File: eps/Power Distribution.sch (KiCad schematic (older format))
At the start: 87 parts, among them Q1 2N7002, Q11 IRF7425, Q12 2N7002, Q13 IRF7425, Q14 IRF7425, Q15 2N7002, Q16 IRF7425, Q17 IRF7425, Q19 IRF7425, Q2 2N7002, Q20 IRF7425, Q21 IRF7425, Q3 IRF7425, Q4 IRF7425, Q5 2N7002, Q6 2N7002, Q9 2N7002, U13 LT6106, U14 LT6106, U15 LT6106, U16 LT6106, U17 LT6106, U18 LT6106, U19 LT6106, U20 LT6106, U21 LT6106

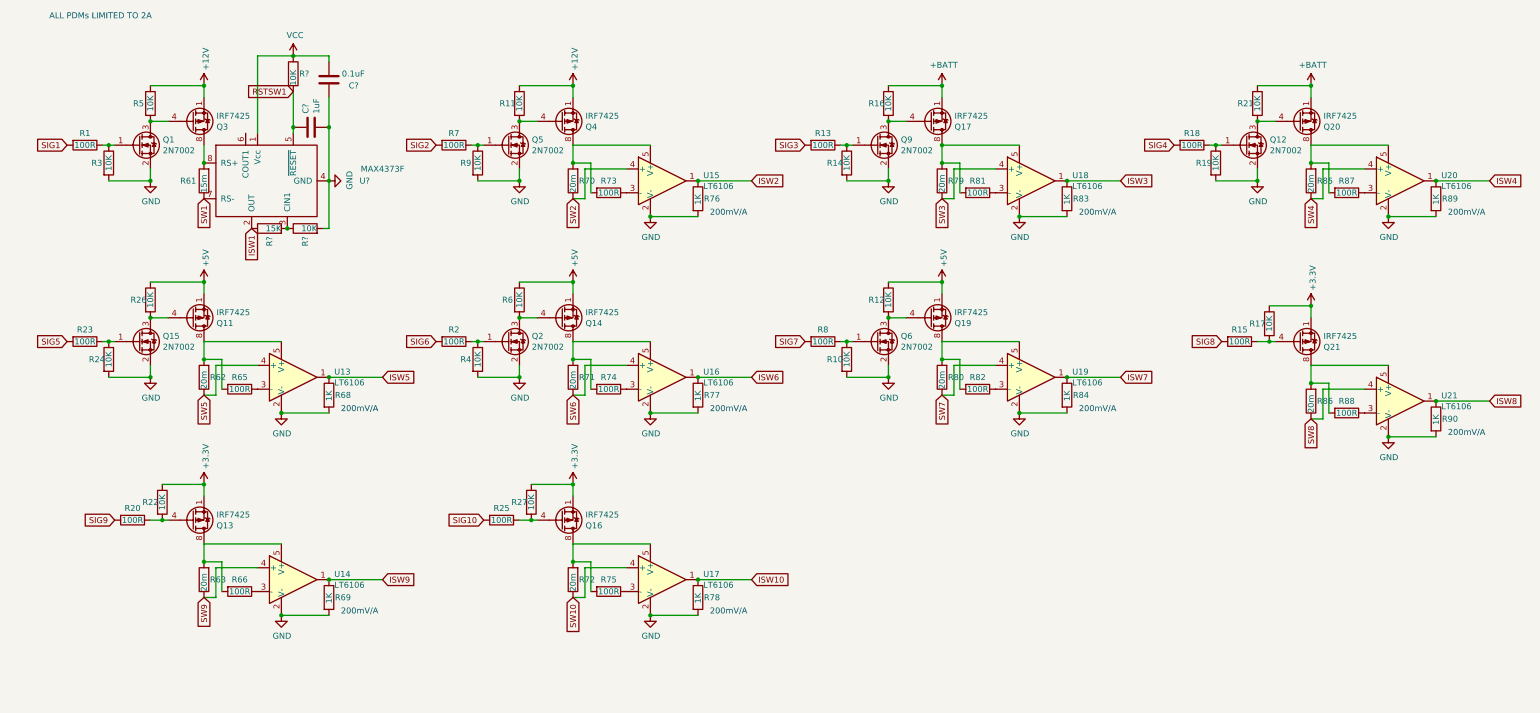
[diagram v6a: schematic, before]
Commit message: implement PDM LCLs
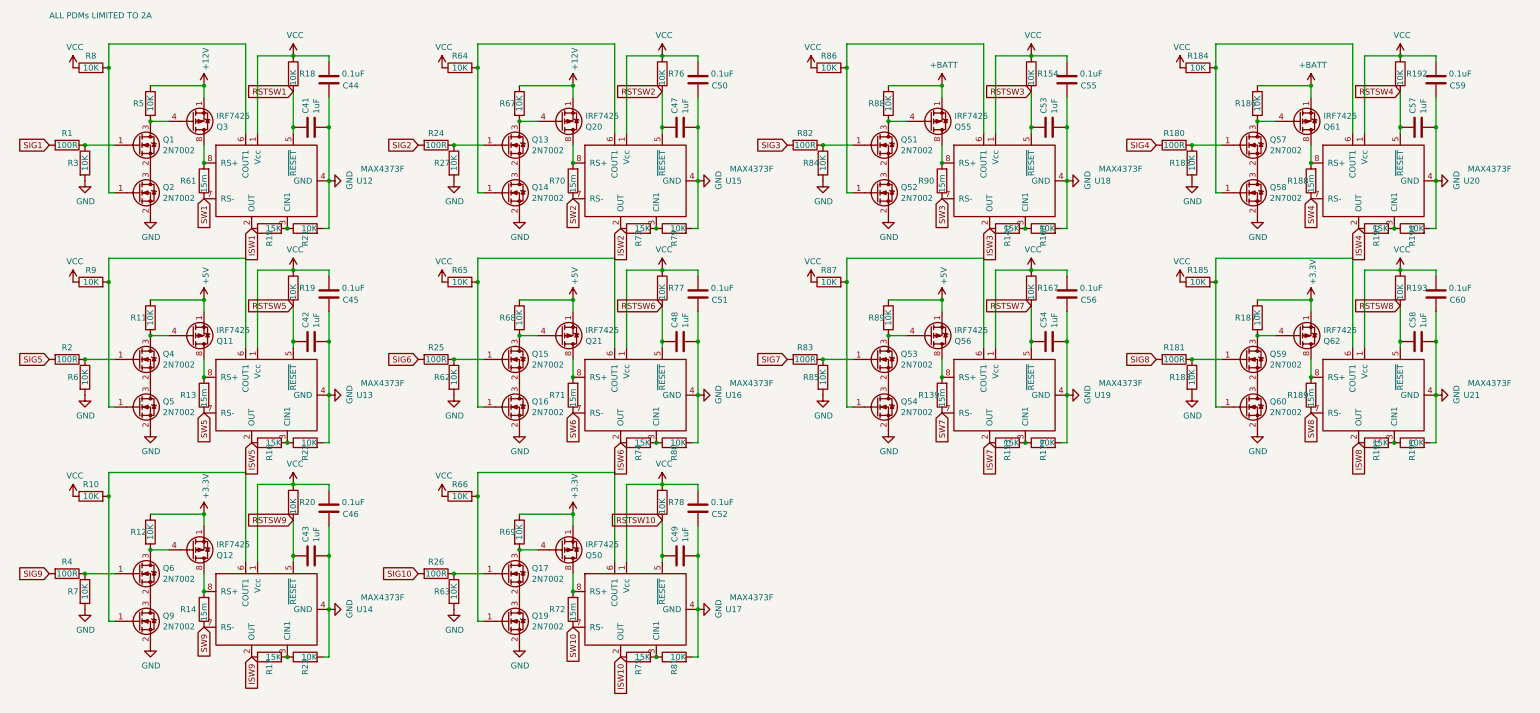
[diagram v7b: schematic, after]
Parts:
- removed Q12: 2N7002, Package_TO_SOT_SMD:SOT-23, symbol Transistor_FET:2N7002
- removed Q13, Q14, Q16, Q17, Q19, Q4: IRF7425, Package_SO:SOIC-8_3.9x4.9mm_P1.27mm, symbol Transistor_FET:IRF7404
- removed R15, R18: 100R, symbol Device:R
- removed R21: 10K, symbol Device:R
- removed U13, U14, U15, U16, U17, U18, U19, U20, U21: LT6106, Package_TO_SOT_SMD:SOT-23-5, symbol Amplifier_Current:LT6106
- added C42, C43, C47, C48, C49, C53, C54, C57, C58: 1uF, symbol Device:C
- added C45, C46, C50, C51, C52, C55, C56, C59, C60: 0.1uF, symbol Device:C
- added Q12, Q50, Q55, Q56, Q61, Q62: IRF7425, Package_SO:SOIC-8_3.9x4.9mm_P1.27mm, symbol Transistor_FET:IRF7404
- added Q13, Q14, Q16, Q17, Q19, Q4, Q51, Q52, Q53, Q54, Q57, Q58, Q59, Q60: 2N7002, Package_TO_SOT_SMD:SOT-23, symbol Transistor_FET:2N7002
- added R139, R188, R189: 15m, symbol Device:R
- added R140, R153, R190, R191: 15K, symbol Device:R
- added R154, R167, R168, R179, R182, R183, R184, R185, R186, R187, R192, R193, R194, R195, R64, R67: 10K, symbol Device:R
- added R180, R181: 100R, symbol Device:R
- added U13, U14, U15, U16, U17, U18, U19, U20, U21: MAX4373F, symbol epslib:MAX4373
- R13: value 100R -> 15m
- R14: value 10K -> 15m
- R16, R17: value 10K -> 15K
- R20, R23, R65, R66, R7, R8, R81, R87, R88: value 100R -> 10K
- R24, R26, R4: value 10K -> 100R
- R62, R63, R79, R80, R85, R86: value 20m -> 10K
- R68, R69, R76, R77, R78, R84, R89: value 1K -> 10K
- R70, R71, R72: value 20m -> 15m
- R73, R74, R75: value 100R -> 15K
- R83: value 1K -> 100R
- R90: value 1K -> 15m
- gave numbers to parts that had none: 6
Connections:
- net +12V: now also Q20.1 (S), Q20.2 (S), Q20.3 (S), R67.1; no longer R11.1
- net +3V3: now also R12.1, R69.1, Q12.1 (S), Q12.2 (S), Q12.3 (S), Q50.1 (S), Q50.2 (S), Q50.3 (S), Q62.1 (S), Q62.2 (S), Q62.3 (S), R187.1; no longer Q21.1 (S), Q21.2 (S), Q21.3 (S), R17.1, R22.1, R27.1
- net +5V: now also Q21.1 (S), Q21.2 (S), Q21.3 (S), R11.1, R68.1, R89.1, Q56.1 (S), Q56.2 (S), Q56.3 (S); no longer R12.1, R26.1, R6.1
- net +BATT: now also R88.1, Q55.1 (S), Q55.2 (S), Q55.3 (S), Q61.1 (S), Q61.2 (S), Q61.3 (S), R186.1; no longer Q20.1 (S), Q20.2 (S), Q20.3 (S), R16.1
- net GND: now also R22.2, R23.2, R27.2, R6.2, R62.2, R63.2, R7.2, R79.2, R80.2, R81.2, R85.2, C42.2, C43.2, C45.1, C46.1, C47.2, C48.2, C49.2, C50.1, C51.1, C52.1, C53.2, C54.2, C55.1, C56.1, C57.2, C58.2, C59.1, C60.1, Q14.2 (S), Q16.2 (S), Q19.2 (S), Q52.2 (S), Q54.2 (S), Q58.2 (S), Q60.2 (S), R168.2, R179.2, R182.2, R183.2, R194.2, R195.2, U13.4 (GND), U14.4 (GND), U15.4 (GND), U16.4 (GND), U17.4 (GND), U18.4 (GND), U19.4 (GND), U20.4 (GND), U21.4 (GND); no longer Q1.2 (S), Q15.2 (S), Q6.2 (S), R10.2, R14.2, R19.2, R24.2, R4.2, R68.2, R69.2, R76.2, R77.2, R78.2, R83.2, R89.2, R9.2, R90.2
- net ISW10: now also R75.1, U17.2 (OUT); no longer R78.1
- net ISW2: now also R73.1, U15.2 (OUT); no longer R76.1
- net ISW3: now also R140.1, U18.2 (OUT); no longer R83.1
- net ISW4: now also R190.1, U20.2 (OUT); no longer R89.1
- net ISW5: now also R16.1, U13.2 (OUT); no longer R68.1
- net ISW6: now also R74.1, U16.2 (OUT); no longer R77.1
- net ISW7: now also R153.1, U19.2 (OUT); no longer R84.1
- net ISW8: now also R191.1, U21.2 (OUT); no longer R90.1
- net ISW9: now also R17.1, U14.2 (OUT); no longer R69.1
- net SIG10: now also R26.2; no longer R25.2
- net SIG2: now also R24.2; no longer R7.2
- net SIG3: now also R82.2; no longer R13.2
- net SIG4: now also R180.2
- net SIG5: now also R2.2; no longer R23.2
- net SIG6: now also R25.2; no longer R2.2
- net SIG7: now also R83.2; no longer R8.2
- net SIG8: now also R181.2
- net SIG9: now also R4.2; no longer R20.2
- net SW10: now also U17.7 (RS-)
- net SW2: now also U15.7 (RS-)
- net SW3: now also R90.1, U18.7 (RS-); no longer R79.1
- net SW4: now also R188.1, U20.7 (RS-); no longer R85.1
- net SW5: now also R13.1, U13.7 (RS-); no longer R62.1
- net SW6: now also U16.7 (RS-)
- net SW7: now also R139.1, U19.7 (RS-); no longer R80.1
- net SW8: now also R189.1, U21.7 (RS-); no longer R86.1
- net SW9: now also R14.1, U14.7 (RS-); no longer R63.1
- net VCC: now also R10.1, R19.1, R20.1, R65.1, R66.1, R76.1, R77.1, R78.1, R8.1, R86.1, R87.1, R9.1, C45.2, C46.2, C50.2, C51.2, C52.2, C55.2, C56.2, C59.2, C60.2, R154.1, R167.1, R184.1, R185.1, R192.1, R193.1, R64.1, U13.1 (Vcc), U14.1 (Vcc), U15.1 (Vcc), U16.1 (Vcc), U17.1 (Vcc), U18.1 (Vcc), U19.1 (Vcc), U20.1 (Vcc), U21.1 (Vcc)
- net at R70.2: now also Q20.5 (D), Q20.6 (D), Q20.7 (D), Q20.8 (D), U15.8 (RS+); no longer R73.2
- net at R81.1: now also R75.2, U17.3 (CIN1)
- net at U12.6 (COUT1): now also Q2.1 (G), R8.2
- net at R16.2: now also R22.1, U13.3 (CIN1); no longer Q9.3 (D)
- net at R11.2: now also Q11.4 (G), Q4.3 (D); no longer Q5.3 (D)
- net at Q20.4 (G): now also Q13.3 (D), R67.2
- net at Q11.5 (D), Q11.6 (D), Q11.7 (D)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: now also R13.2, U13.8 (RS+); no longer R62.2, R65.2
- net at Q2.3 (D): now also Q1.2 (S); no longer R6.2
- net at R71.2: now also Q21.5 (D), Q21.6 (D), Q21.7 (D), Q21.8 (D), U16.8 (RS+); no longer R74.2
- net at Q6.3 (D), R12.2: now also Q12.4 (G)
- net at Q21.4 (G): now also Q15.3 (D), R68.2; no longer R17.2
- net at R66.2: now also Q19.1 (G), U17.6 (COUT1); no longer R63.2
- net at R25.1: now also Q15.1 (G), R62.1; no longer R27.2
- net at R72.2: now also Q50.5 (D), Q50.6 (D), Q50.7 (D), Q50.8 (D), U17.8 (RS+); no longer R75.2
- net at R82.1: now also R84.1, Q51.1 (G)
- new net: Q13.1 (G), R24.1, R27.1
- new net: Q13.2 (S), Q14.3 (D)
- new net: R73.2, R79.1, U15.3 (CIN1)
- new net: Q14.1 (G), R64.2, U15.6 (COUT1)
- new net: Q51.3 (D), Q55.4 (G), R88.2
- new net: Q55.5 (D), Q55.6 (D), Q55.7 (D), Q55.8 (D), R90.2, U18.8 (RS+)
- new net: Q51.2 (S), Q52.3 (D)
- new net: R140.2, R168.1, U18.3 (CIN1)
- new net: Q52.1 (G), R86.2, U18.6 (COUT1)
- new net: Q57.3 (D), Q61.4 (G), R186.2
- new net: Q61.5 (D), Q61.6 (D), Q61.7 (D), Q61.8 (D), R188.2, U20.8 (RS+)
- new net: Q57.1 (G), R180.1, R182.1
- new net: Q57.2 (S), Q58.3 (D)
- new net: R190.2, R194.1, U20.3 (CIN1)
- new net: Q58.1 (G), R184.2, U20.6 (COUT1)
- new net: Q4.1 (G), R2.1, R6.1
- new net: Q4.2 (S), Q5.3 (D)
- new net: Q5.1 (G), R9.2, U13.6 (COUT1)
- new net: Q15.2 (S), Q16.3 (D)
- new net: R74.2, R80.1, U16.3 (CIN1)
- new net: Q16.1 (G), R65.2, U16.6 (COUT1)
- new net: Q53.3 (D), Q56.4 (G), R89.2
- new net: Q56.5 (D), Q56.6 (D), Q56.7 (D), Q56.8 (D), R139.2, U19.8 (RS+)
- new net: Q53.1 (G), R83.1, R85.1
- new net: Q53.2 (S), Q54.3 (D)
- new net: R153.2, R179.1, U19.3 (CIN1)
- new net: Q54.1 (G), R87.2, U19.6 (COUT1)
- new net: Q59.3 (D), Q62.4 (G), R187.2
- new net: Q62.5 (D), Q62.6 (D), Q62.7 (D), Q62.8 (D), R189.2, U21.8 (RS+)
- new net: Q59.1 (G), R181.1, R183.1
- new net: Q59.2 (S), Q60.3 (D)
- new net: R191.2, R195.1, U21.3 (CIN1)
- new net: Q60.1 (G), R185.2, U21.6 (COUT1)
- new net: Q12.5 (D), Q12.6 (D), Q12.7 (D), Q12.8 (D), R14.2, U14.8 (RS+)
- new net: Q6.1 (G), R4.1, R7.1
- new net: Q6.2 (S), Q9.3 (D)
- new net: R17.2, R23.1, U14.3 (CIN1)
- new net: Q9.1 (G), R10.2, U14.6 (COUT1)
- new net: Q17.3 (D), Q50.4 (G), R69.2
- new net: Q17.1 (G), R26.1, R63.1
- new net: Q17.2 (S), Q19.3 (D)
- new net RSTSW10: C49.1, R78.2, U17.5 (~RESET)
- new net RSTSW2: C47.1, R76.2, U15.5 (~RESET)
- new net RSTSW3: C53.1, R154.2, U18.5 (~RESET)
- new net RSTSW4: C57.1, R192.2, U20.5 (~RESET)
- new net RSTSW5: C42.1, R19.2, U13.5 (~RESET)
- new net RSTSW6: C48.1, R77.2, U16.5 (~RESET)
- new net RSTSW7: C54.1, R167.2, U19.5 (~RESET)
- new net RSTSW8: C58.1, R193.2, U21.5 (~RESET)
- new net RSTSW9: C43.1, R20.2, U14.5 (~RESET)
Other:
- note removed: "200mV/A\n"
- moved on the sheet: R1, R3

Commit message: update pcbnew
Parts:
- C41, C42, C43, C44, C45, C46, C47, C48, C49, C50, C51, C52, C53, C54, C55, C56, C57, C58, C59, C60: footprint (none) -> Capacitor_SMD:C_0805_2012Metric_Pad1.18x1.45mm_HandSolder
- R1, R10, R11, R12, R13, R139, R14, R140, R15, R153, R154, R16, R167, R168, R17, R179, R18, R180, R181, R182, R183, R184, R185, R186, R187, R188, R189, R19, R190, R191, R192, R193, R194, R195, R2, R20, R21, R22, R23, R24, R25, R26, R27, R3, R4, R5, R6, R61, R62, R63, R64, R65, R66, R67, R68, R69, R7, R70, R71, R72, R73, R74, R75, R76, R77, R78, R79, R8, R80, R81, R82, R83, R84, R85, R86, R87, R88, R89, R9, R90: footprint (none) -> Resistor_SMD:R_0805_2012Metric_Pad1.20x1.40mm_HandSolder
